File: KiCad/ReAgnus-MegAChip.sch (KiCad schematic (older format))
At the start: 29 parts, among them J3 Conn_02x01, J4 Conn_01x01, J5 Conn_01x01, J6 Conn_01x01, J7 Conn_01x01, U1 PLCC-84-Plug, U2 LM1117-3.3, U3 SN74CBTD16210, U4 SN74CBTD16210, U5 SN74CBTD16210, U6 SN74CBTD16210, U8 74LVC1G07, U9 Agnus_TH_plug_pins

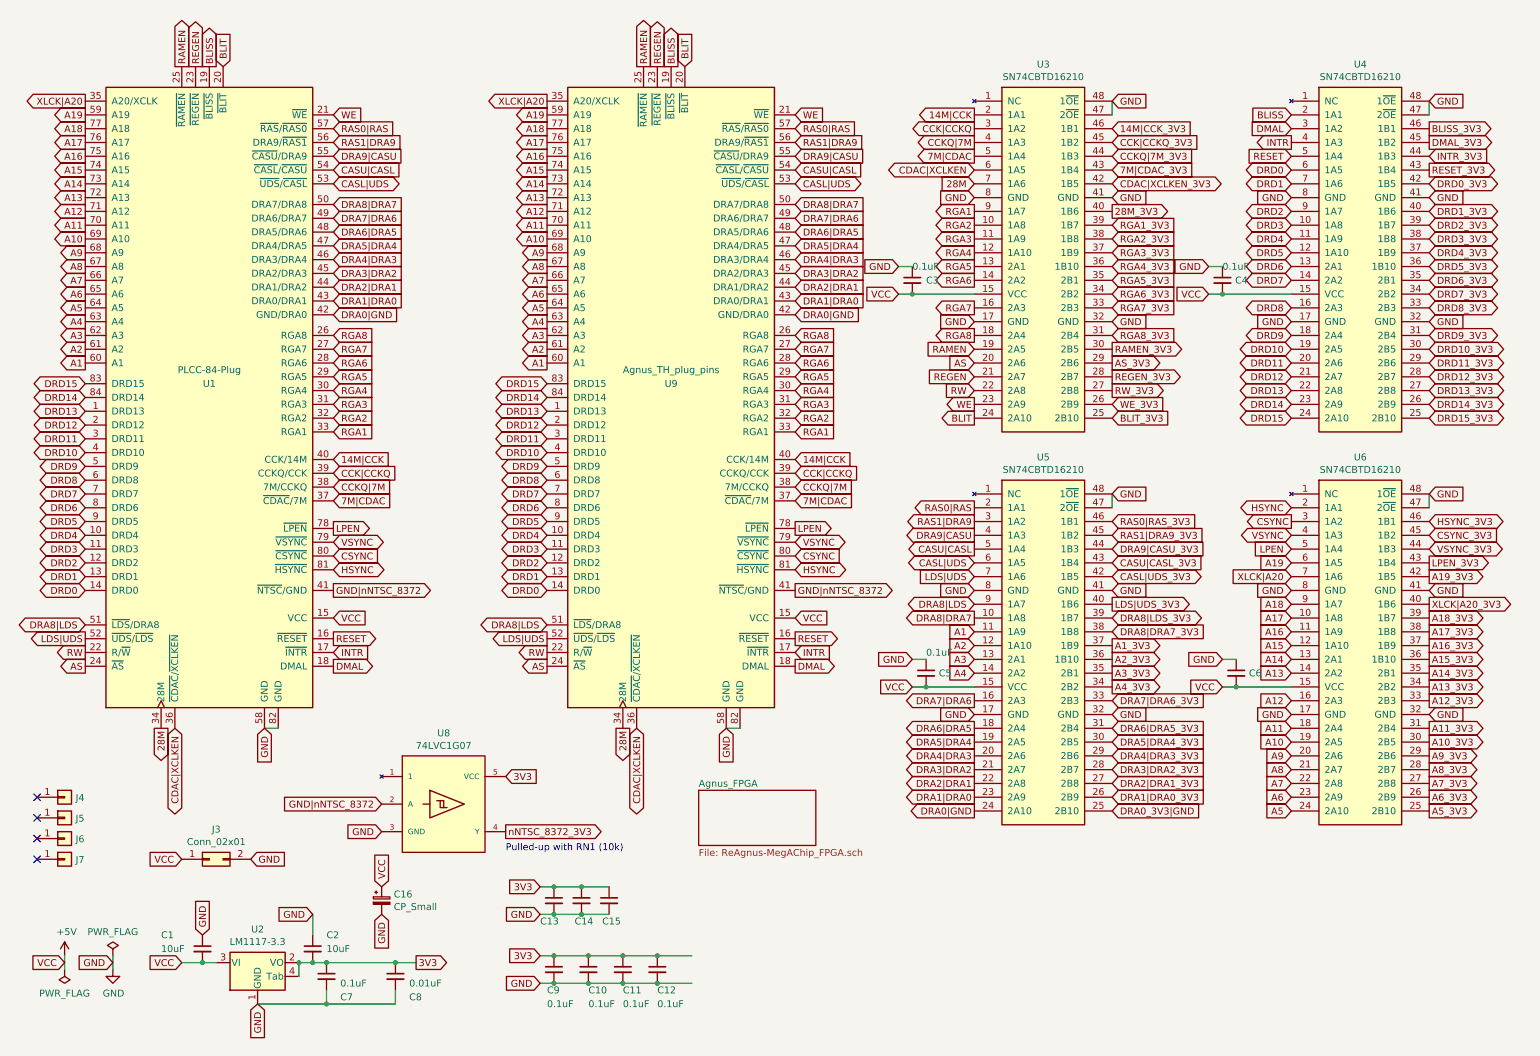
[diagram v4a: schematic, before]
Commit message: renaming of Capacitors
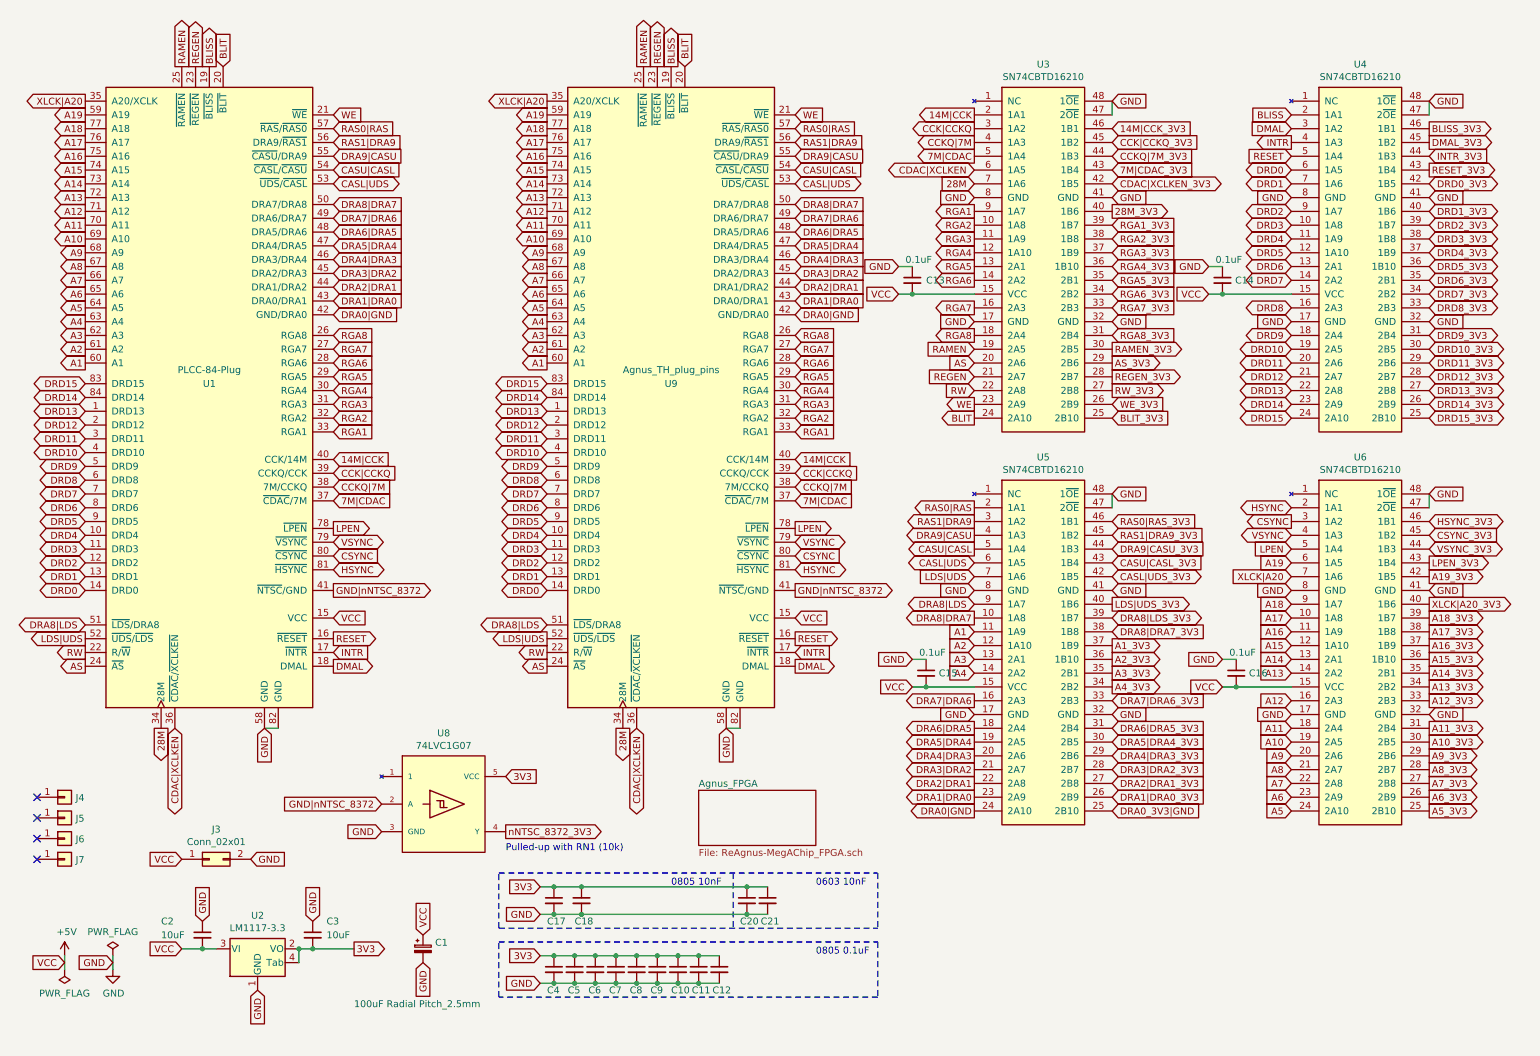
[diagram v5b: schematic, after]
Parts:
- added C10, C11, C12, C9: 0.1uF, Capacitor_SMD:C_0805_2012Metric_Pad1.15x1.40mm_HandSolder, symbol Device:C_Small
- C1: renamed from C16; value CP_Small -> 100uF Radial Pitch_2.5mm
- C16: renamed from C6; value C_Small -> 0.1uF
- C17: renamed from C11; value 0.1uF -> 0.01uF
- C7: renamed from C13; value 0.01uF -> 0.1uF
- renumbered C3 to C13, C4 to C14, C5 to C15, C14 to C18, C1 to C2, C8 to C20, C15 to C21, C2 to C3, C7 to C4, C9 to C5, C10 to C6, C12 to C8
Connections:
- wire segments 48 -> 51
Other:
- note added: "0603 10nF"
- note added: "0805 0.1uF"
- note added: "0805 10nF"
- moved on the sheet: C1, C17, C2, C20, C21, C3, C4, C5, C6, C7, C8, U2

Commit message: more routing and placing components
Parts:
- added C19: 0.01uF, Capacitor_SMD:C_0805_2012Metric_Pad1.15x1.40mm_HandSolder, symbol Device:C_Small
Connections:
- net 3V3: now also C19.1
- net GND: now also C19.2
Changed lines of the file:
@@
 	4000 6750 6750 6750
 Wire Wire Line
-	4600 6850 5800 6850
-Wire Wire Line
-	4600 7050 5800 7050
+	4600 6850 4800 6850
+Wire Wire Line
+	4600 7050 4800 7050
 Text Notes 6300 6850 0    50   ~ 0
 0603 10nF
@@
 	5450 7550 5600 7550
 Connection ~ 5450 7550
+$Comp
+L Device:C_Small C19
+U 1 1 63426A79
+P 4800 6950
+AR Path="/63426A79" Ref="C19"  Part="1"
+AR Path="/632D3BDF/63426A79" Ref="C?"  Part="1"
+AR Path="/632F104D/63426A79" Ref="C?"  Part="1"
+F 0 "C19" H 4750 6800 50  0000 L CNN
+F 1 "0.01uF" H 4750 6700 50  0001 L CNN
+F 2 "Capacitor_SMD:C_0805_2012Metric_Pad1.15x1.40mm_HandSolder" H 4800 6950 50  0001 C CNN
+F 3 "~" H 4800 6950 50  0001 C CNN
+	1    4800 6950
+	1    0    0    -1
+$EndComp
+Connection ~ 4800 6850
+Wire Wire Line
+	4800 6850 5800 6850
+Connection ~ 4800 7050
+Wire Wire Line
+	4800 7050 5800 7050
 $EndSCHEMATC

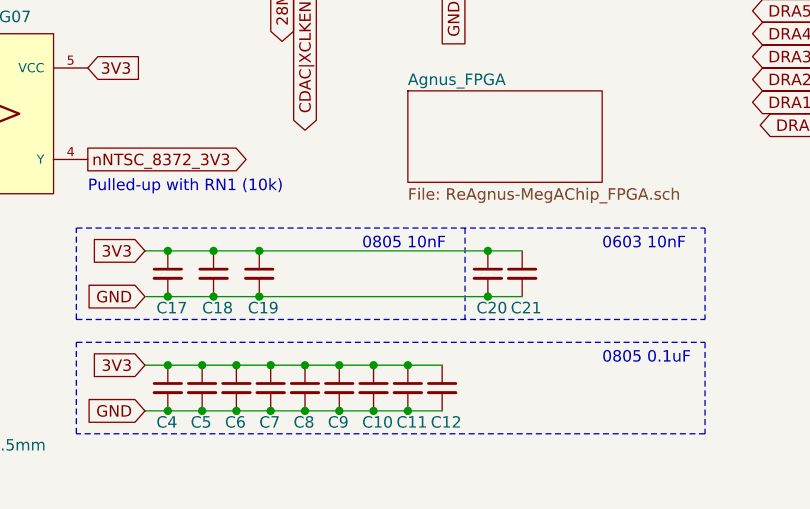
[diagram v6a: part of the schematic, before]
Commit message: added Oscillator X1 for SDRAM and GCLKT_1 pin on FPGA
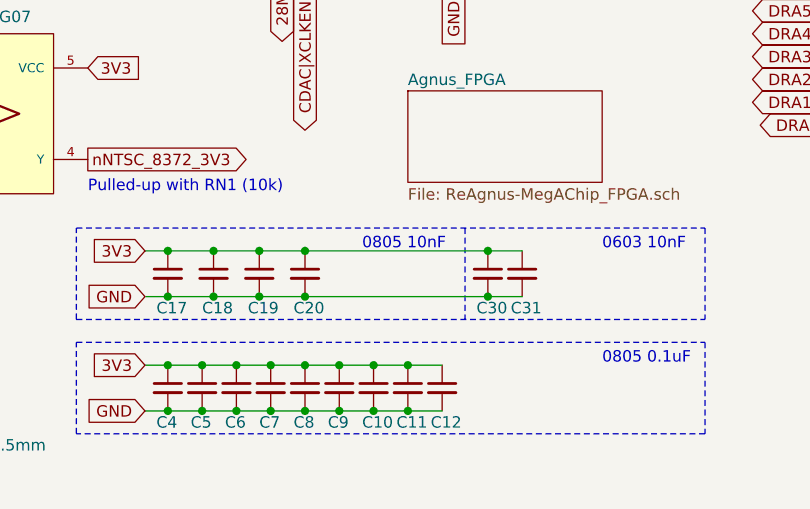
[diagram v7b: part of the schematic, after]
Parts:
- added C20: 0.01uF, Capacitor_SMD:C_0805_2012Metric_Pad1.15x1.40mm_HandSolder, symbol Device:C_Small
- renumbered C20 to C30, C21 to C31
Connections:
- net 3V3: now also C20.1
- net GND: now also C20.2
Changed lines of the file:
@@
 GND
 $Comp
-L Device:C_Small C20
+L Device:C_Small C30
 U 1 1 631E37EB
 P 5800 6950
-AR Path="/631E37EB" Ref="C20"  Part="1"
+AR Path="/631E37EB" Ref="C30"  Part="1"
 AR Path="/632D3BDF/631E37EB" Ref="C?"  Part="1"
 AR Path="/632F104D/631E37EB" Ref="C?"  Part="1"
-F 0 "C20" H 5750 6800 50  0000 L CNN
+F 0 "C30" H 5750 6800 50  0000 L CNN
 F 1 "0.01uF" H 5550 6900 50  0001 L CNN
 F 2 "Capacitor_SMD:C_0603_1608Metric_Pad1.05x0.95mm_HandSolder" H 5800 6950 50  0001 C CNN
@@
 	4300 6850 4400 6850
 $Comp
-L Device:C_Small C21
+L Device:C_Small C31
 U 1 1 632C350C
 P 5950 6950
-AR Path="/632C350C" Ref="C21"  Part="1"
+AR Path="/632C350C" Ref="C31"  Part="1"
 AR Path="/632D3BDF/632C350C" Ref="C?"  Part="1"
 AR Path="/632F104D/632C350C" Ref="C?"  Part="1"
-F 0 "C21" H 5900 6800 50  0000 L CNN
+F 0 "C31" H 5900 6800 50  0000 L CNN
 F 1 "0.01uF" H 5900 6700 50  0001 L CNN
 F 2 "Capacitor_SMD:C_0603_1608Metric_Pad1.05x0.95mm_HandSolder" H 5950 6950 50  0001 C CNN
@@
 Connection ~ 4800 6850
 Wire Wire Line
-	4800 6850 5800 6850
+	4800 6850 5000 6850
 Connection ~ 4800 7050
 Wire Wire Line
-	4800 7050 5800 7050
+	4800 7050 5000 7050
+$Comp
+L Device:C_Small C20
+U 1 1 6370FC11
+P 5000 6950
+AR Path="/6370FC11" Ref="C20"  Part="1"
+AR Path="/632D3BDF/6370FC11" Ref="C?"  Part="1"
+AR Path="/632F104D/6370FC11" Ref="C?"  Part="1"
+F 0 "C20" H 4950 6800 50  0000 L CNN
+F 1 "0.01uF" H 4950 6700 50  0001 L CNN
+F 2 "Capacitor_SMD:C_0805_2012Metric_Pad1.15x1.40mm_HandSolder" H 5000 6950 50  0001 C CNN
+F 3 "~" H 5000 6950 50  0001 C CNN
+	1    5000 6950
+	1    0    0    -1
+$EndComp
+Connection ~ 5000 6850
+Wire Wire Line
+	5000 6850 5800 6850
+Connection ~ 5000 7050
+Wire Wire Line
+	5000 7050 5800 7050
 $EndSCHEMATC

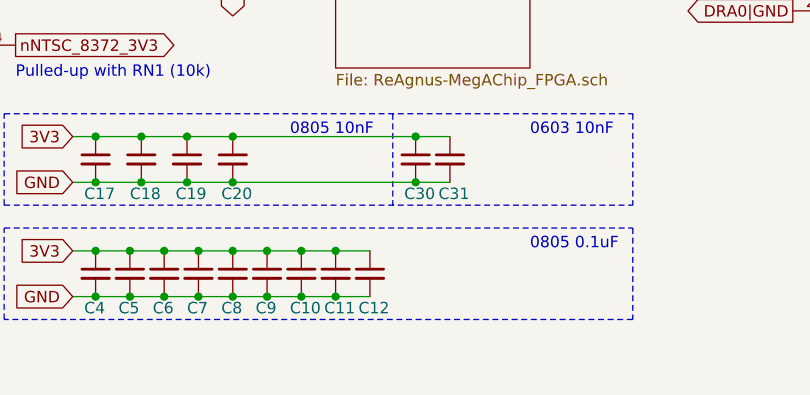
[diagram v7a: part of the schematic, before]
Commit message: added decoupling cap for U11
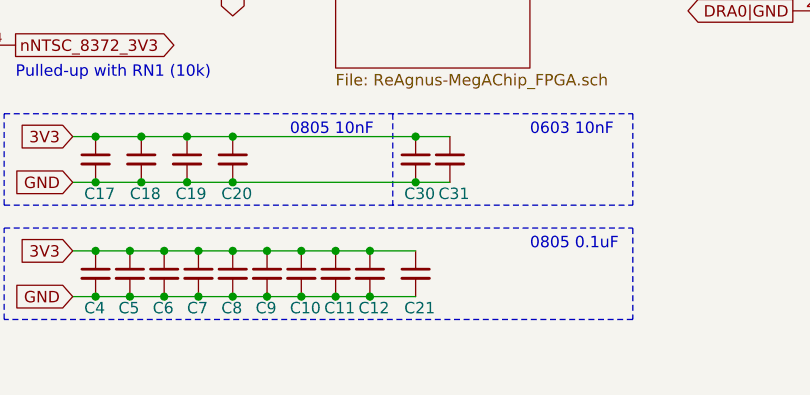
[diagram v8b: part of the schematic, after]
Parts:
- added C21: 0.1uF, Capacitor_SMD:C_0805_2012Metric_Pad1.15x1.40mm_HandSolder, symbol Device:C_Small
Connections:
- net 3V3: now also C21.1
- net GND: now also C21.2
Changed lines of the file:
@@
 Wire Wire Line
 	5000 7050 5800 7050
+$Comp
+L Device:C_Small C21
+U 1 1 638ABF1F
+P 5800 7450
+AR Path="/638ABF1F" Ref="C21"  Part="1"
+AR Path="/632D3BDF/638ABF1F" Ref="C?"  Part="1"
+AR Path="/632F104D/638ABF1F" Ref="C?"  Part="1"
+F 0 "C21" H 5750 7300 50  0000 L CNN
+F 1 "0.1uF" H 5800 7200 50  0001 L CNN
+F 2 "Capacitor_SMD:C_0805_2012Metric_Pad1.15x1.40mm_HandSolder" H 5800 7450 50  0001 C CNN
+F 3 "~" H 5800 7450 50  0001 C CNN
+	1    5800 7450
+	1    0    0    -1
+$EndComp
+Wire Wire Line
+	5600 7350 5800 7350
+Connection ~ 5600 7350
+Wire Wire Line
+	5600 7550 5800 7550
+Connection ~ 5600 7550
 $EndSCHEMATC
